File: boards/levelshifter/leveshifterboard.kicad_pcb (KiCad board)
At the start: 2 copper layers, 82.5 x 43.2 mm, 40 parts, among them J1 RJ45, P1 CONN_2, P2 CONN_7, Q1 IRLR110, Q2 NDS355, SW1 SW_PUSH, U1 LM358, U2 SN74LVC1G74, U3 74HCT125, U4 TS2937

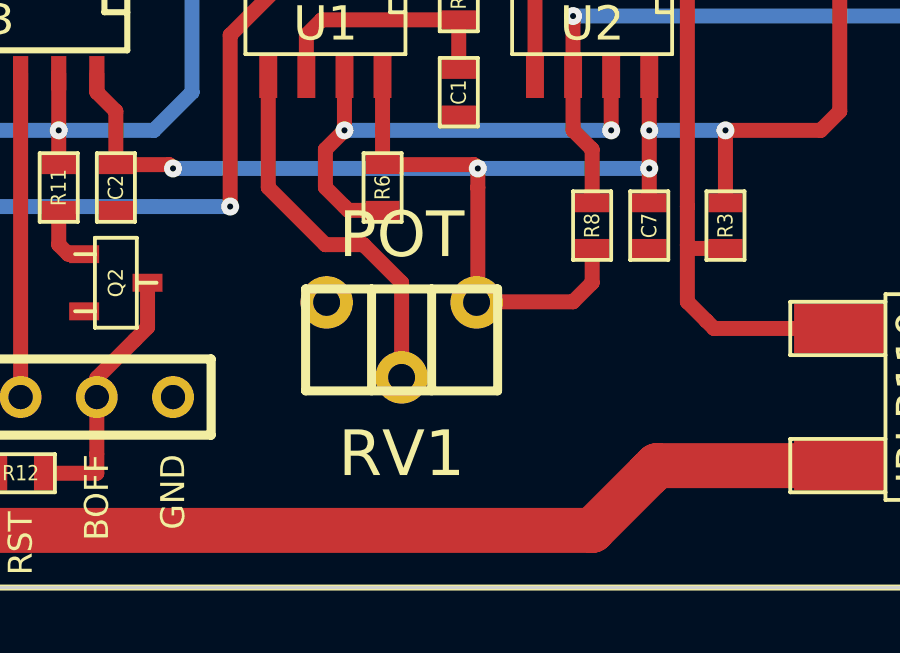
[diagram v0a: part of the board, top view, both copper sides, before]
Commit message: Semifinal version of enclosure lids
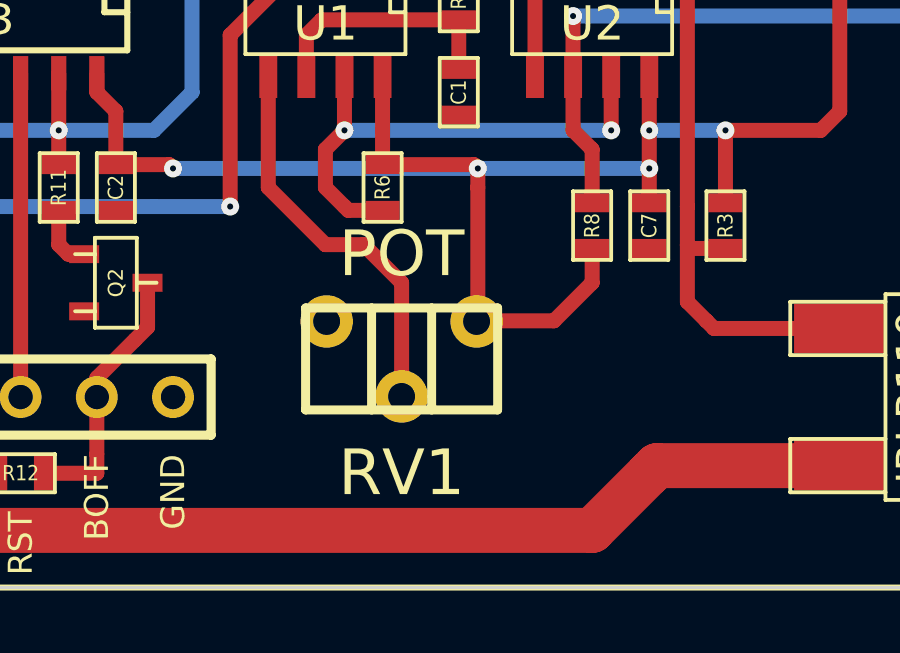
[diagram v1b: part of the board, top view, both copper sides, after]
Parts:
- moved RV1 0.64 mm to (168.3, 80.0)
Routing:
- net +5V: track 85.7 -> 86.6 mm
- net N-0000012: track 12.6 -> 13.2 mm
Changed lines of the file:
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@@
   )
   (module trimmer_piher_pt6xh (layer F.Cu)
-    (at 168.275 79.375)
+    (at 168.275 80.01)
     (descr "trimmer, Piher PT6-xH")
     (tags trimmer)
@@
   (via (at 160.655 73.66) (size 0.6) (drill 0.2) (layers F.Cu B.Cu) (net 3))
   (segment (start 174.625 76.327) (end 174.625 77.47) (width 0.5) (layer F.Cu) (net 3))
-  (segment (start 170.79468 78.105) (end 173.99 78.105) (width 0.5) (layer F.Cu) (net 3))
-  (segment (start 173.99 78.105) (end 174.625 77.47) (width 0.5) (layer F.Cu) (net 3))
-  (segment (start 170.79468 78.105) (end 170.77436 78.12532) (width 0.5) (layer F.Cu) (net 3))
+  (segment (start 170.79468 78.74) (end 173.355 78.74) (width 0.5) (layer F.Cu) (net 3) (status 10))
+  (segment (start 173.355 78.74) (end 174.625 77.47) (width 0.5) (layer F.Cu) (net 3))
+  (segment (start 170.79468 78.74) (end 170.77436 78.76032) (width 0.5) (layer F.Cu) (net 3) (status 30))
   (via (at 176.53 73.66) (size 0.6) (drill 0.2) (layers F.Cu B.Cu) (net 3))
   (via (at 170.815 73.66) (size 0.6) (drill 0.2) (layers F.Cu B.Cu) (net 3))
@@
   (segment (start 176.53 73.66) (end 176.53 72.39) (width 0.5) (layer F.Cu) (net 3) (status 10))
   (segment (start 170.815 73.66) (end 170.688 73.533) (width 0.5) (layer F.Cu) (net 3))
-  (segment (start 170.815 78.08468) (end 170.815 74.295) (width 0.5) (layer F.Cu) (net 3))
+  (segment (start 170.815 78.71968) (end 170.815 74.295) (width 0.5) (layer F.Cu) (net 3) (status 10))
   (segment (start 170.815 74.295) (end 170.815 73.66) (width 0.5) (layer F.Cu) (net 3))
-  (segment (start 170.77436 78.12532) (end 170.815 78.08468) (width 0.5) (layer F.Cu) (net 3))
+  (segment (start 170.77436 78.76032) (end 170.815 78.71968) (width 0.5) (layer F.Cu) (net 3) (status 30))
   (segment (start 170.688 73.533) (end 167.64 73.533) (width 0.5) (layer F.Cu) (net 3))
   (segment (start 158.115 70.485) (end 158.115 71.12) (width 0.5) (layer F.Cu) (net 3))
@@
   (segment (start 135.89 48.26) (end 135.89 55.88) (width 1.5) (layer F.Cu) (net 13))
   (segment (start 188.722 59.69) (end 190.373 59.69) (width 0.5) (layer F.Cu) (net 14) (status 10))
-  (segment (start 168.275 80.62468) (end 168.275 77.47) (width 0.5) (layer F.Cu) (net 15))
+  (segment (start 168.275 81.25968) (end 168.275 77.47) (width 0.5) (layer F.Cu) (net 15) (status 10))
   (segment (start 163.83 74.295) (end 165.735 76.2) (width 0.5) (layer F.Cu) (net 15))
   (segment (start 165.735 76.2) (end 167.005 76.2) (width 0.5) (layer F.Cu) (net 15))
